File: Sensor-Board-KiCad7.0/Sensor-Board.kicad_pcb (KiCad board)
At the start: 2 copper layers, 75.4 x 75.4 mm, 134 parts, among them J2 B04B-XASK-1, U1 OPA396DCKT, U10 BME680, U11 OPA396DCKT, U12 OPA396DCKT, U14 OPA396DCKT, U15 MMBFJ177LT1, U16 MMBFJ177LT1, U17 MMBFJ177LT1, U18 NAU7802SGI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

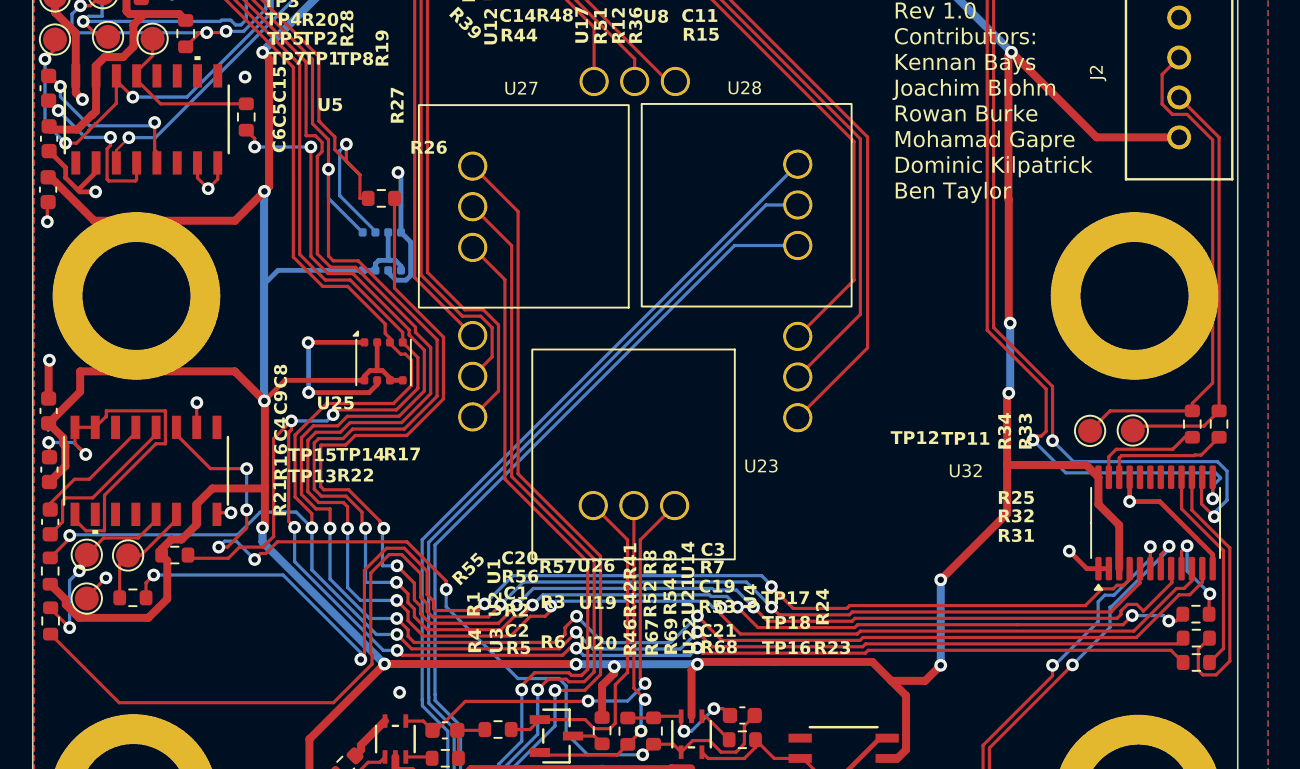
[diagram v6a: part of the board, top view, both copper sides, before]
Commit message: Added PU resistors to multiplexer
Added pull-up resistor to RESET as well as decoupling capacitors to digital multiplexer. Fixed routing intersection errors.
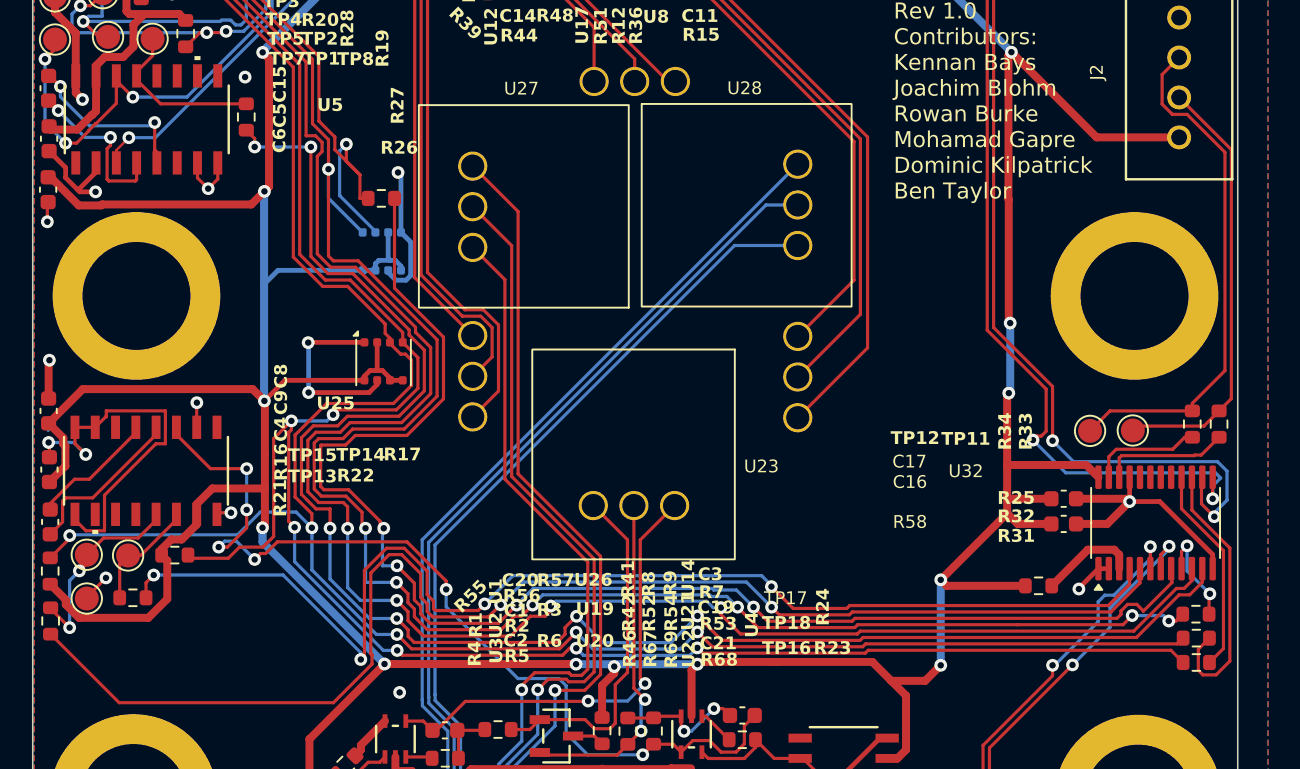
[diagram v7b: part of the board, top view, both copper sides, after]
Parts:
- added C16: 100nF, Capacitor_SMD:C_0603_1608Metric, F.Cu at (164.5, 109.9)
- added C17: 100nF, Capacitor_SMD:C_0603_1608Metric, F.Cu at (164.5, 108.3)
- added R58: 4.7k, Resistor_SMD:R_0603_1608Metric, F.Cu at (162.9, 113.8)
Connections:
- U32 pad 3: +3.3V -> Net-(U32-~{RESET})
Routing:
- net GND: track 189.5 -> 196.3 mm
- net Net-(U32-~{RESET}): track 0.00 -> 6.16 mm
- net +3.3V: track 470.7 -> 473.3 mm
- net MUX_SDA: track 31.9 -> 32.5 mm
- net MUX_SCL: track 27.2 -> 27.8 mm

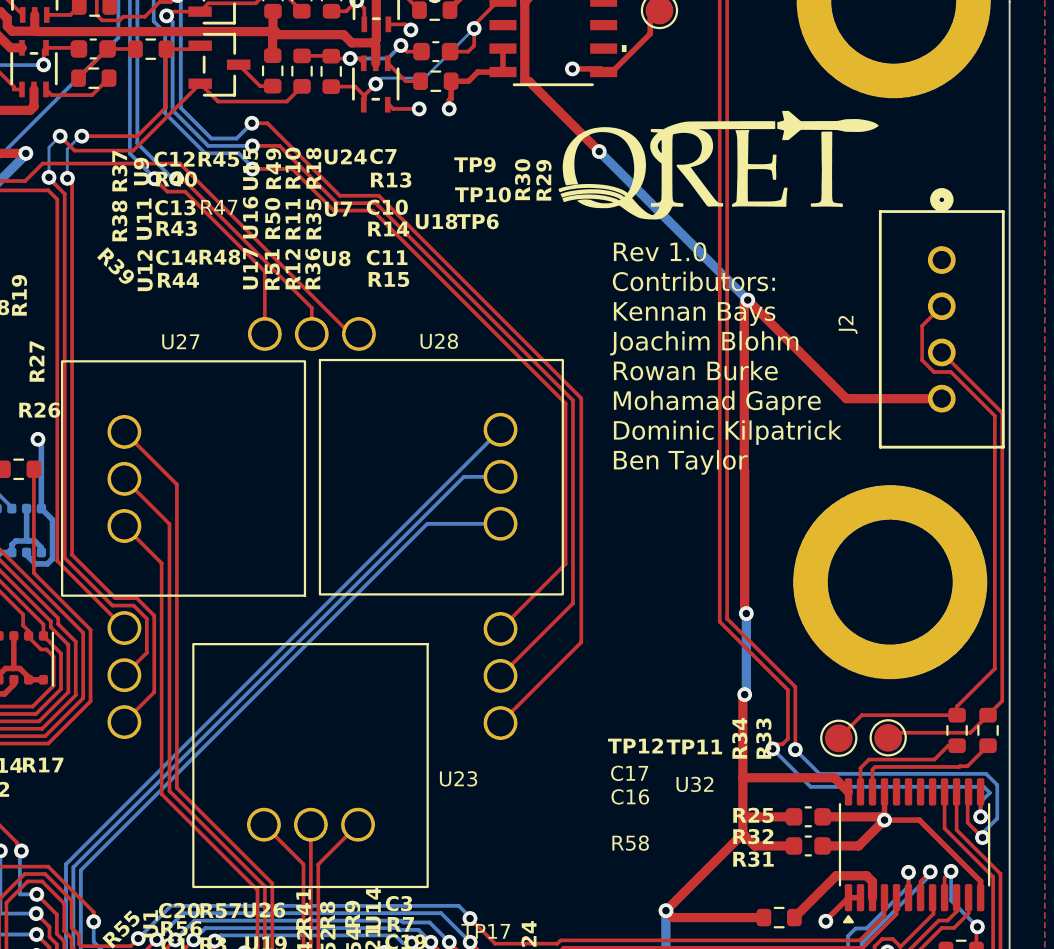
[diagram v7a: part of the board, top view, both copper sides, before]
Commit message: Added board name
Added board name and increased Echem socket diameter to 1.46mm to account for tolerances.
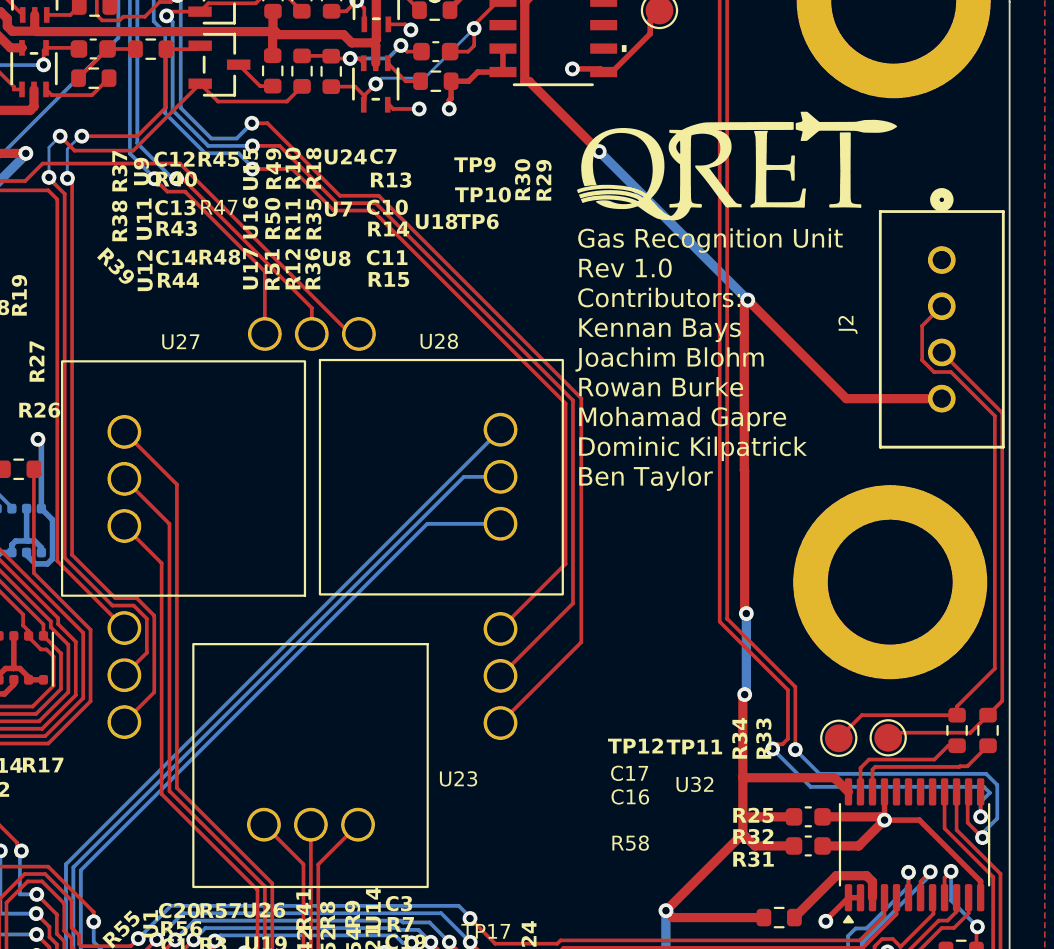
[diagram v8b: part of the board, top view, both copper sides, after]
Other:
- board text added: "Gas Recognition Unit Rev 1.0 Contributors: Kennan Bays Joachim Blohm Rowan Burke Mohamad Gapre Dominic Kilpatrick Ben Taylor"
- board text removed: "Rev 1.0 Contributors: Kennan Bays Joachim Blohm Rowan Burke Mohamad Gapre Dominic Kilpatrick Ben Taylor"
